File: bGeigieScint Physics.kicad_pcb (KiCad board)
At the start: 4 copper layers, 33 x 30.5 mm, 18 parts, among them IC1 MICROFJ-60035-TSV-TR, P1 Header-Male-2.54_2x2, P2 Header-Male-2.54_2x2, U1 TMP116xxDRV, U2 AT24CS01-STUM

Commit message: Added OpenGamma and Mii-SiD project in Kicad files.
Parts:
- moved IC1 1.03 mm to (147.4, 91.4)
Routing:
- net /3V3: track 59.7 -> 97.0 mm
- net GND: track 6.79 -> 13.8 mm, vias 1 -> 4
- net Net-(IC1-CATHODE_1): track 34.7 -> 30.7 mm, vias 2 -> 3
- net Net-(C1-Pad1): track 14.4 -> 18.1 mm
- net /Vbias: track 19.4 -> 23.0 mm, vias 2 -> 0
- net /PA17: track 22.9 -> 22.0 mm
- net /PA16: track 26.9 -> 27.0 mm, vias 2 -> 0

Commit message: This version of Antigravity is no longer supported. Please update to receive the latest features!
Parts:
- moved P1 3.19 mm to (142.9, 98.4)
- moved P2 3.19 mm to (151.1, 98.4)
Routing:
- net Net-(IC1-CATHODE_1): track 30.7 -> 40.2 mm
- net /SiPM_A: track 9.56 -> 18.7 mm
- net /3V3: track 97.0 -> 92.3 mm
- net /PA16: track 27.0 -> 24.2 mm
- net /PA17: track 22.0 -> 20.1 mm
- net /Vbias: track 23.0 -> 21.7 mm
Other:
- board text added: "bGeigieScint Sensor-board V0.9A"
- board text removed: "bGeigieScint Sensor-board V0.9"

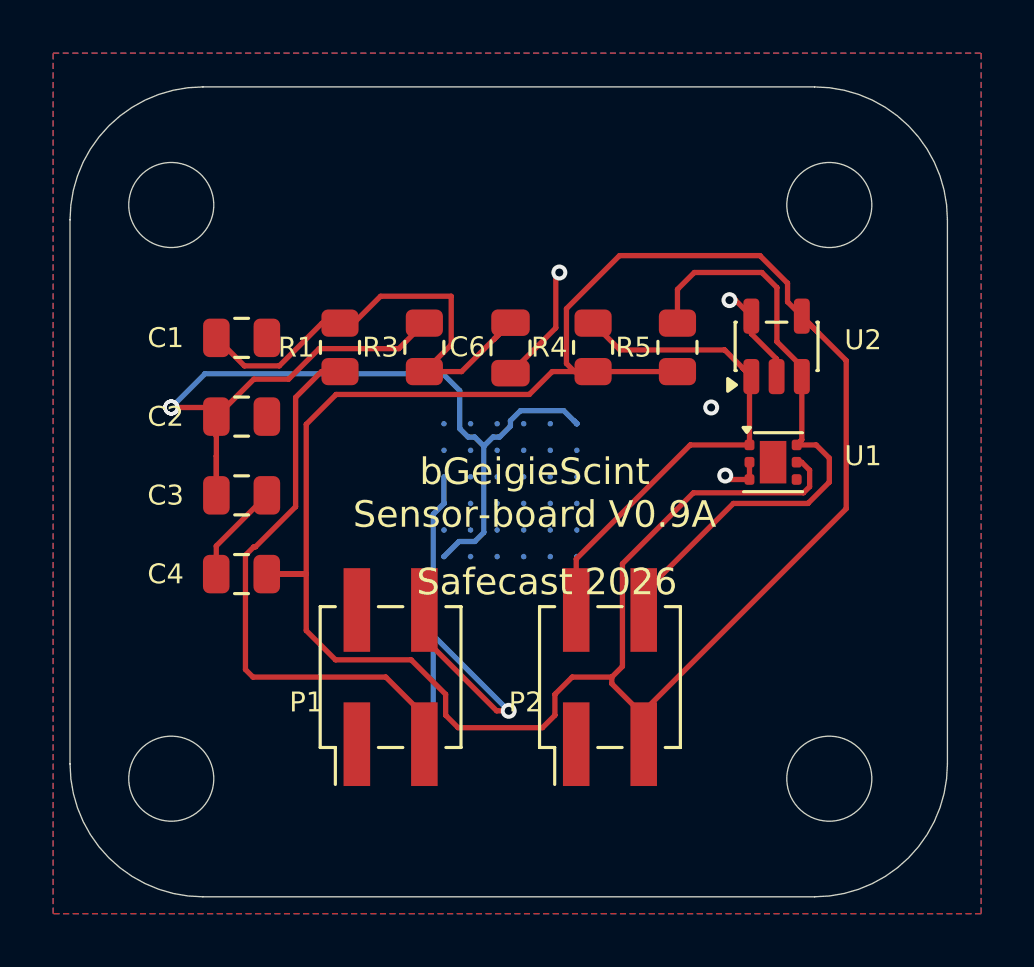
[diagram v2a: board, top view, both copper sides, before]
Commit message: - Added initial entries for various components including capacitors, resistors, and headers.T right angle counts
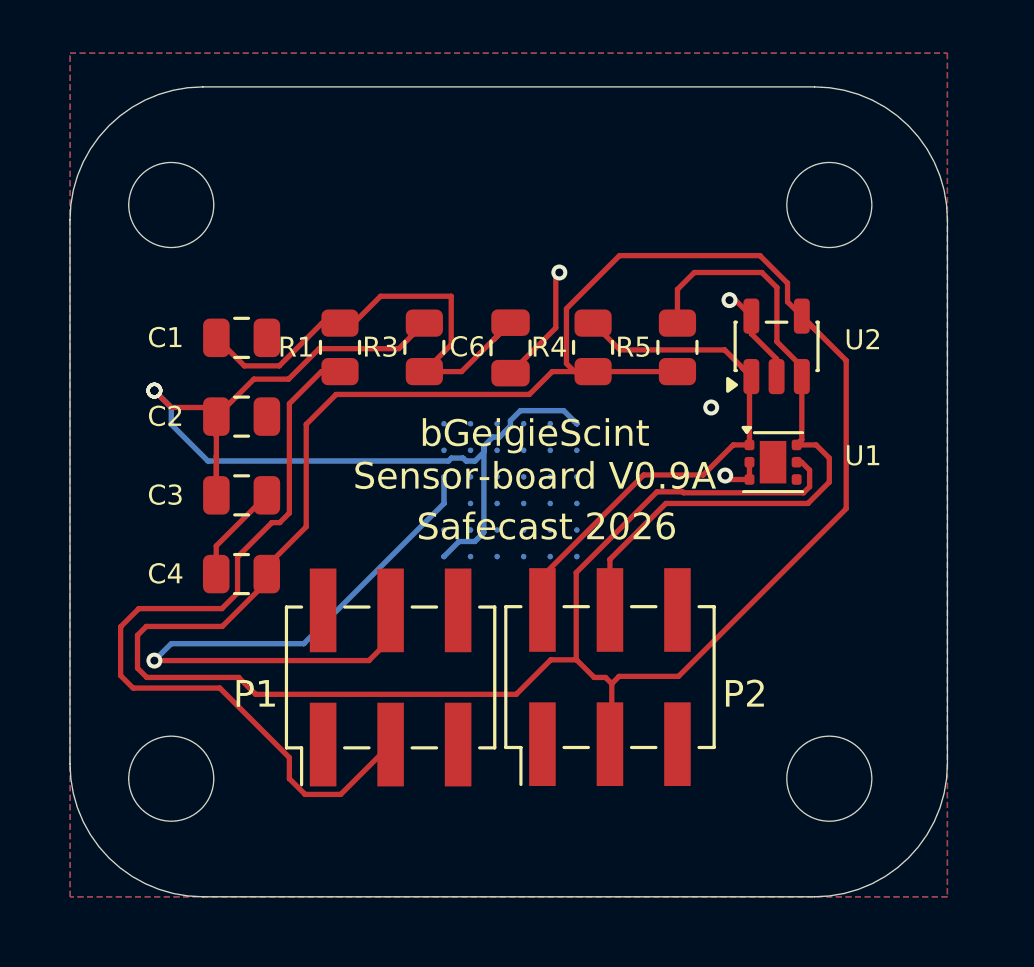
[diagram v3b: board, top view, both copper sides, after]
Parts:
- P1, P2: footprint Connector_PinHeader_2.54mm:PinHeader_2x02_P2.54mm_Vertical_SMD -> Connector_PinHeader_2.54mm:PinHeader_2x03_P2.54mm_Vertical_SMD
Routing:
- net /Vbias: track 21.7 -> 30.5 mm
- net /3V3: track 92.3 -> 99.1 mm
- net /SiPM_A: track 18.7 -> 24.7 mm
- net /PA16: track 24.2 -> 26.2 mm
- net Net-(IC1-CATHODE_1): track 40.2 -> 41.2 mm
- net /PA17: track 20.1 -> 21.0 mm
